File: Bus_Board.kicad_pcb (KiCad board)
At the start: 2 copper layers, 295.9 x 39.4 mm, 44 parts, among them J1 +5V, J10 Conn_02x05_Odd_Even, J11 Conn_02x08_Odd_Even, J12 Conn_02x05_Odd_Even, J13 Conn_02x08_Odd_Even, J14 Conn_02x05_Odd_Even, J15 Conn_02x08_Odd_Even, J16 Conn_02x05_Odd_Even, J17 Conn_02x08_Odd_Even, J18 Conn_02x05_Odd_Even, J19 Conn_02x08_Odd_Even, J2 +12V, J20 Conn_02x05_Odd_Even, J21 Conn_02x08_Odd_Even, J22 Conn_02x05_Odd_Even, J23 Conn_02x08_Odd_Even, J24 Conn_02x05_Odd_Even, J25 +5V, J26 +12V, J27 GND, J28 -12V, J3 GND, J4 -12V, J5 Conn_02x08_Odd_Even, J6 Conn_02x05_Odd_Even, J7 Conn_02x08_Odd_Even, J8 Conn_02x05_Odd_Even, J9 Conn_02x08_Odd_Even

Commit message: Fix orientation of connectors and some other parts
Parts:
- moved J17 18.0 mm to (73.7, 80.0), turned to 180 degrees
- moved J5 18.0 mm to (-101.0, 80.0), turned to 180 degrees
- moved J11 18.0 mm to (-25.4, 80.0), turned to 180 degrees
- moved J13 18.0 mm to (-0.75, 80.0), turned to 180 degrees
- moved J19 18.0 mm to (97.6, 80.0), turned to 180 degrees
- moved J21 18.0 mm to (120.4, 80.0), turned to 180 degrees
- moved J9 18.0 mm to (-50.8, 80.0), turned to 180 degrees
- moved J23 18.0 mm to (143.3, 80.0), turned to 180 degrees
- moved J7 18.0 mm to (-76.2, 80.0), turned to 180 degrees
- moved J15 17.9 mm to (50.2, 80.0), turned to 180 degrees
- moved J24 10.5 mm to (155.5, 80.0), turned to 180 degrees
- moved J12 10.5 mm to (-13.2, 80.0), turned to 180 degrees
- moved J18 10.5 mm to (85.6, 80.0), turned to 180 degrees
- moved J20 10.5 mm to (109.0, 80.0), turned to 180 degrees
- moved J8 10.5 mm to (-63.5, 80.0), turned to 180 degrees
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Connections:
- C3 pad 1: -12V -> GND
- C3 pad 2: GND -> -12V
- D3 pad 1: GND -> Net-(R3-Pad1)
- D3 pad 2: Net-(D3-Pad2) -> GND
- J10 pad 1: +12V -> -12V
- J10 pad 10: -12V -> +12V
- J10 pad 2: +12V -> -12V
- J10 pad 9: -12V -> +12V
- J11 pad 1: Net-(J7-Pad1) -> -12V
- J11 pad 10: GND -> +12V
- J11 pad 11: GND -> +5V
- J11 pad 12: GND -> +5V
- J11 pad 13: GND -> Net-(J11-Pad13)
- J11 pad 14: GND -> Net-(J11-Pad13)
- J11 pad 15: -12V -> Net-(J11-Pad15)
- J11 pad 16: -12V -> Net-(J11-Pad15)
- J11 pad 2: Net-(J7-Pad1) -> -12V
- J11 pad 3: Net-(J7-Pad3) -> GND
- J11 pad 4: Net-(J7-Pad3) -> GND
- J11 pad 5: +5V -> GND
- J11 pad 6: +5V -> GND
- J11 pad 7: +12V -> GND
- J11 pad 8: +12V -> GND
- J11 pad 9: GND -> +12V
- J12 pad 1: +12V -> -12V
- J12 pad 10: -12V -> +12V
- J12 pad 2: +12V -> -12V
- J12 pad 9: -12V -> +12V
- J13 pad 1: Net-(J7-Pad1) -> -12V
- J13 pad 10: GND -> +12V
- J13 pad 11: GND -> +5V
- J13 pad 12: GND -> +5V
- J13 pad 13: GND -> Net-(J11-Pad13)
- J13 pad 14: GND -> Net-(J11-Pad13)
- J13 pad 15: -12V -> Net-(J11-Pad15)
- J13 pad 16: -12V -> Net-(J11-Pad15)
- J13 pad 2: Net-(J7-Pad1) -> -12V
- J13 pad 3: Net-(J7-Pad3) -> GND
- J13 pad 4: Net-(J7-Pad3) -> GND
- J13 pad 5: +5V -> GND
- J13 pad 6: +5V -> GND
- J13 pad 7: +12V -> GND
- J13 pad 8: +12V -> GND
- J13 pad 9: GND -> +12V
- J14 pad 1: +12V -> -12V
- J14 pad 10: -12V -> +12V
- J14 pad 2: +12V -> -12V
- J14 pad 9: -12V -> +12V
- J15 pad 1: Net-(J19-Pad1) -> -12V
- J15 pad 10: GND -> +12V
- J15 pad 11: GND -> +5V
- J15 pad 12: GND -> +5V
- J15 pad 13: GND -> Net-(J15-Pad13)
- J15 pad 14: GND -> Net-(J15-Pad13)
- J15 pad 15: -12V -> Net-(J15-Pad15)
- J15 pad 16: -12V -> Net-(J15-Pad15)
- J15 pad 2: Net-(J19-Pad1) -> -12V
- J15 pad 3: Net-(J19-Pad3) -> GND
- J15 pad 4: Net-(J19-Pad3) -> GND
- J15 pad 5: +5V -> GND
- J15 pad 6: +5V -> GND
- J15 pad 7: +12V -> GND
- J15 pad 8: +12V -> GND
- J15 pad 9: GND -> +12V
- J16 pad 1: +12V -> -12V
- J16 pad 10: -12V -> +12V
- J16 pad 2: +12V -> -12V
- J16 pad 9: -12V -> +12V
- J17 pad 1: Net-(J19-Pad1) -> -12V
- J17 pad 10: GND -> +12V
- J17 pad 11: GND -> +5V
- J17 pad 12: GND -> +5V
- J17 pad 13: GND -> Net-(J15-Pad13)
- J17 pad 14: GND -> Net-(J15-Pad13)
- J17 pad 15: -12V -> Net-(J15-Pad15)
- J17 pad 16: -12V -> Net-(J15-Pad15)
- J17 pad 2: Net-(J19-Pad1) -> -12V
- J17 pad 3: Net-(J19-Pad3) -> GND
- J17 pad 4: Net-(J19-Pad3) -> GND
- J17 pad 5: +5V -> GND
- J17 pad 6: +5V -> GND
- J17 pad 7: +12V -> GND
- J17 pad 8: +12V -> GND
- J17 pad 9: GND -> +12V
- J18 pad 1: +12V -> -12V
- J18 pad 10: -12V -> +12V
- J18 pad 2: +12V -> -12V
- J18 pad 9: -12V -> +12V
- J19 pad 1: Net-(J19-Pad1) -> -12V
- J19 pad 10: GND -> +12V
- J19 pad 11: GND -> +5V
- J19 pad 12: GND -> +5V
- J19 pad 13: GND -> Net-(J15-Pad13)
- J19 pad 14: GND -> Net-(J15-Pad13)
- J19 pad 15: -12V -> Net-(J15-Pad15)
- J19 pad 16: -12V -> Net-(J15-Pad15)
- J19 pad 2: Net-(J19-Pad1) -> -12V
- J19 pad 3: Net-(J19-Pad3) -> GND
- J19 pad 4: Net-(J19-Pad3) -> GND
- J19 pad 5: +5V -> GND
- J19 pad 6: +5V -> GND
- J19 pad 7: +12V -> GND
- J19 pad 8: +12V -> GND
- J19 pad 9: GND -> +12V
- J20 pad 1: +12V -> -12V
- J20 pad 10: -12V -> +12V
- J20 pad 2: +12V -> -12V
- J20 pad 9: -12V -> +12V
- J21 pad 1: Net-(J19-Pad1) -> -12V
- J21 pad 10: GND -> +12V
- J21 pad 11: GND -> +5V
- J21 pad 12: GND -> +5V
- J21 pad 13: GND -> Net-(J15-Pad13)
- J21 pad 14: GND -> Net-(J15-Pad13)
- J21 pad 15: -12V -> Net-(J15-Pad15)
- J21 pad 16: -12V -> Net-(J15-Pad15)
- J21 pad 2: Net-(J19-Pad1) -> -12V
- J21 pad 3: Net-(J19-Pad3) -> GND
- J21 pad 4: Net-(J19-Pad3) -> GND
- J21 pad 5: +5V -> GND
- J21 pad 6: +5V -> GND
- J21 pad 7: +12V -> GND
- J21 pad 8: +12V -> GND
- J21 pad 9: GND -> +12V
- J22 pad 1: +12V -> -12V
- J22 pad 10: -12V -> +12V
- J22 pad 2: +12V -> -12V
- J22 pad 9: -12V -> +12V
- J23 pad 1: Net-(J19-Pad1) -> -12V
- J23 pad 10: GND -> +12V
- J23 pad 11: GND -> +5V
- J23 pad 12: GND -> +5V
- J23 pad 13: GND -> Net-(J15-Pad13)
- J23 pad 14: GND -> Net-(J15-Pad13)
- J23 pad 15: -12V -> Net-(J15-Pad15)
- J23 pad 16: -12V -> Net-(J15-Pad15)
- J23 pad 2: Net-(J19-Pad1) -> -12V
- J23 pad 3: Net-(J19-Pad3) -> GND
- J23 pad 4: Net-(J19-Pad3) -> GND
- J23 pad 5: +5V -> GND
- J23 pad 6: +5V -> GND
- J23 pad 7: +12V -> GND
- J23 pad 8: +12V -> GND
- J23 pad 9: GND -> +12V
- J24 pad 1: +12V -> -12V
- J24 pad 10: -12V -> +12V
- J24 pad 2: +12V -> -12V
- J24 pad 9: -12V -> +12V
- J5 pad 1: Net-(J7-Pad1) -> -12V
- J5 pad 10: GND -> +12V
- J5 pad 11: GND -> +5V
- J5 pad 12: GND -> +5V
- J5 pad 13: GND -> Net-(J11-Pad13)
- J5 pad 14: GND -> Net-(J11-Pad13)
- J5 pad 15: -12V -> Net-(J11-Pad15)
- J5 pad 16: -12V -> Net-(J11-Pad15)
- J5 pad 2: Net-(J7-Pad1) -> -12V
- J5 pad 3: Net-(J7-Pad3) -> GND
- J5 pad 4: Net-(J7-Pad3) -> GND
- J5 pad 5: +5V -> GND
- J5 pad 6: +5V -> GND
- J5 pad 7: +12V -> GND
- J5 pad 8: +12V -> GND
- J5 pad 9: GND -> +12V
- J6 pad 1: +12V -> -12V
- J6 pad 10: -12V -> +12V
- J6 pad 2: +12V -> -12V
- J6 pad 9: -12V -> +12V
- J7 pad 1: Net-(J7-Pad1) -> -12V
- J7 pad 10: GND -> +12V
- J7 pad 11: GND -> +5V
- J7 pad 12: GND -> +5V
- J7 pad 13: GND -> Net-(J11-Pad13)
- J7 pad 14: GND -> Net-(J11-Pad13)
- J7 pad 15: -12V -> Net-(J11-Pad15)
- J7 pad 16: -12V -> Net-(J11-Pad15)
- J7 pad 2: Net-(J7-Pad1) -> -12V
- J7 pad 3: Net-(J7-Pad3) -> GND
- J7 pad 4: Net-(J7-Pad3) -> GND
- J7 pad 5: +5V -> GND
- J7 pad 6: +5V -> GND
- J7 pad 7: +12V -> GND
- J7 pad 8: +12V -> GND
- J7 pad 9: GND -> +12V
- J8 pad 1: +12V -> -12V
- J8 pad 10: -12V -> +12V
- J8 pad 2: +12V -> -12V
- J8 pad 9: -12V -> +12V
- J9 pad 1: Net-(J7-Pad1) -> -12V
- J9 pad 10: GND -> +12V
- J9 pad 11: GND -> +5V
- J9 pad 12: GND -> +5V
- J9 pad 13: GND -> Net-(J11-Pad13)
- J9 pad 14: GND -> Net-(J11-Pad13)
- J9 pad 15: -12V -> Net-(J11-Pad15)
- J9 pad 16: -12V -> Net-(J11-Pad15)
- J9 pad 2: Net-(J7-Pad1) -> -12V
- J9 pad 3: Net-(J7-Pad3) -> GND
- J9 pad 4: Net-(J7-Pad3) -> GND
- J9 pad 5: +5V -> GND
- J9 pad 6: +5V -> GND
- J9 pad 7: +12V -> GND
- J9 pad 8: +12V -> GND
- J9 pad 9: GND -> +12V
- R3 pad 1: Net-(D3-Pad2) -> Net-(R3-Pad1)
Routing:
- net Net-(J7-Pad3): track 102.9 -> 0.00 mm
- net Net-(J7-Pad1): track 102.9 -> 0.00 mm
- net Net-(J11-Pad15): track 0.00 -> 102.9 mm
- net Net-(J11-Pad13): track 0.00 -> 102.9 mm
- net Net-(J19-Pad3): track 95.2 -> 0.00 mm
- net Net-(J19-Pad1): track 95.2 -> 0.00 mm
- net Net-(J15-Pad15): track 0.00 -> 95.2 mm
- net Net-(J15-Pad13): track 0.00 -> 95.2 mm
- net Net-(R3-Pad1): track 0.00 -> 6.76 mm
- net Net-(D3-Pad2): track 6.76 -> 0.00 mm

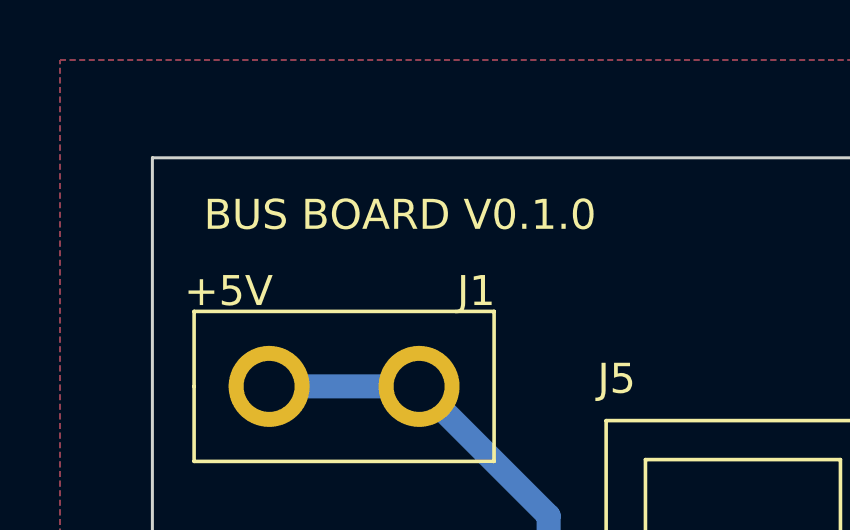
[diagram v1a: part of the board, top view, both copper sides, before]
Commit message: Fix Bug, add thermal reliefs to groundplane
Bugfix: reverse polarity of C3 and D3
Add thermal reliefs in ground plane for easier soldering
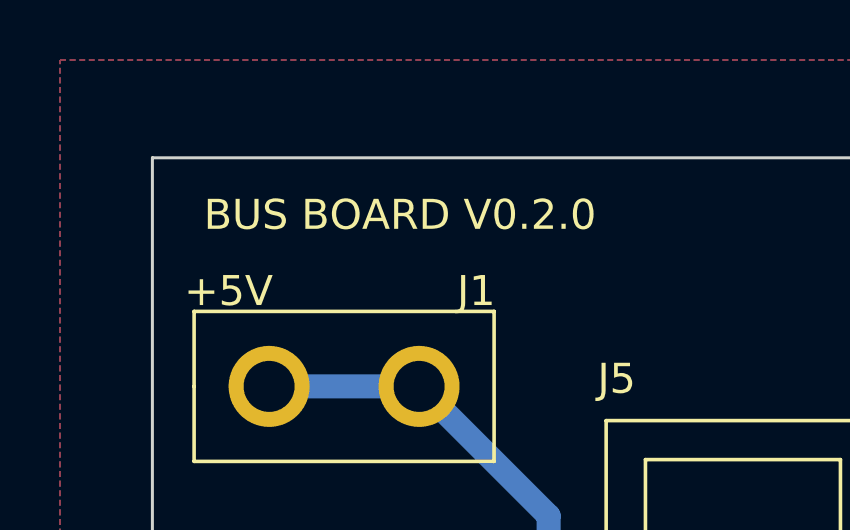
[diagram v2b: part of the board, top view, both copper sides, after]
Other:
- board text added: "BUS BOARD V0.2.0"
- board text removed: "BUS BOARD V0.1.0"
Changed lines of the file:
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@@
     (effects (font (size 1 1) (thickness 0.15)))
   )
-  (gr_text "BUS BOARD V0.1.0" (at -113.665 50.165) (layer "F.SilkS")
+  (gr_text "BUS BOARD V0.2.0" (at -113.665 50.165) (layer "F.SilkS")
     (effects (font (size 1 1) (thickness 0.15)))
   )
@@
     (connect_pads (clearance 0.508))
     (min_thickness 0.254) (filled_areas_thickness no)
-    (fill yes (thermal_gap 0.508) (thermal_bridge_width 0.508))
+    (fill (thermal_gap 0.508) (thermal_bridge_width 0.508))
     (polygon
       (pts

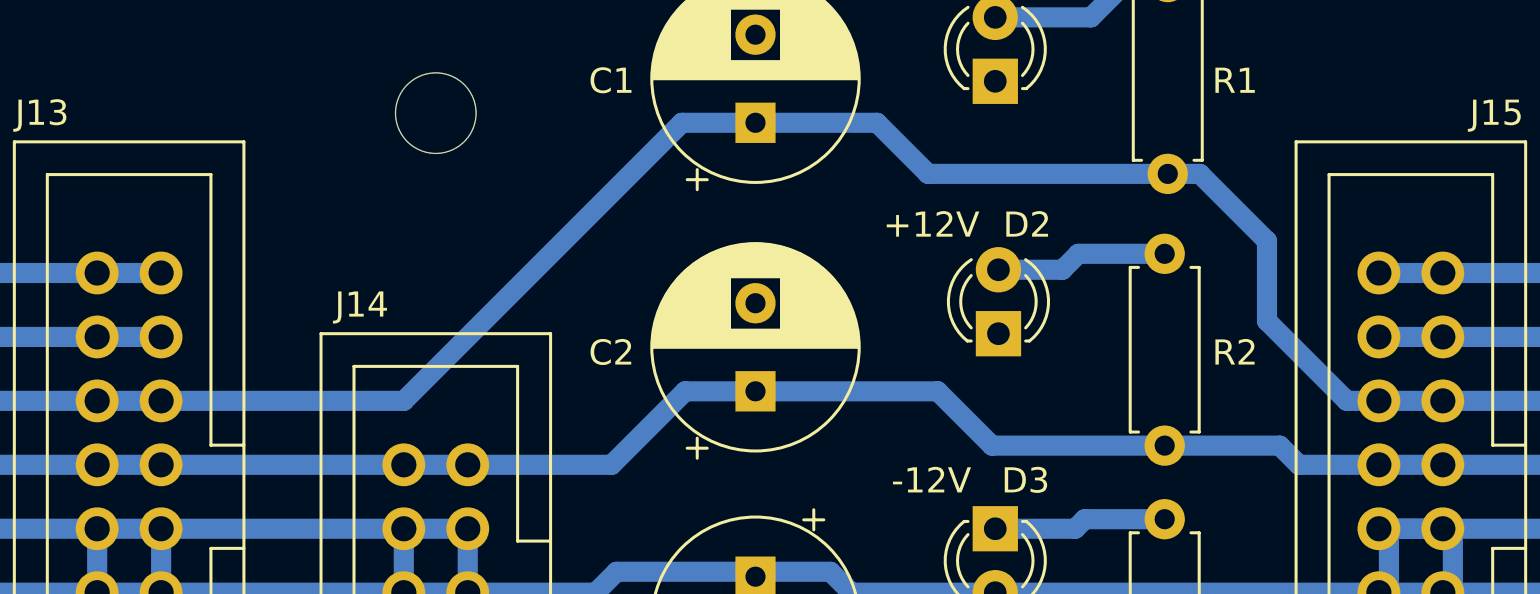
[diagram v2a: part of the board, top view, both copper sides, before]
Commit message: Connect CV and GATE lines, add ljcpcb order number
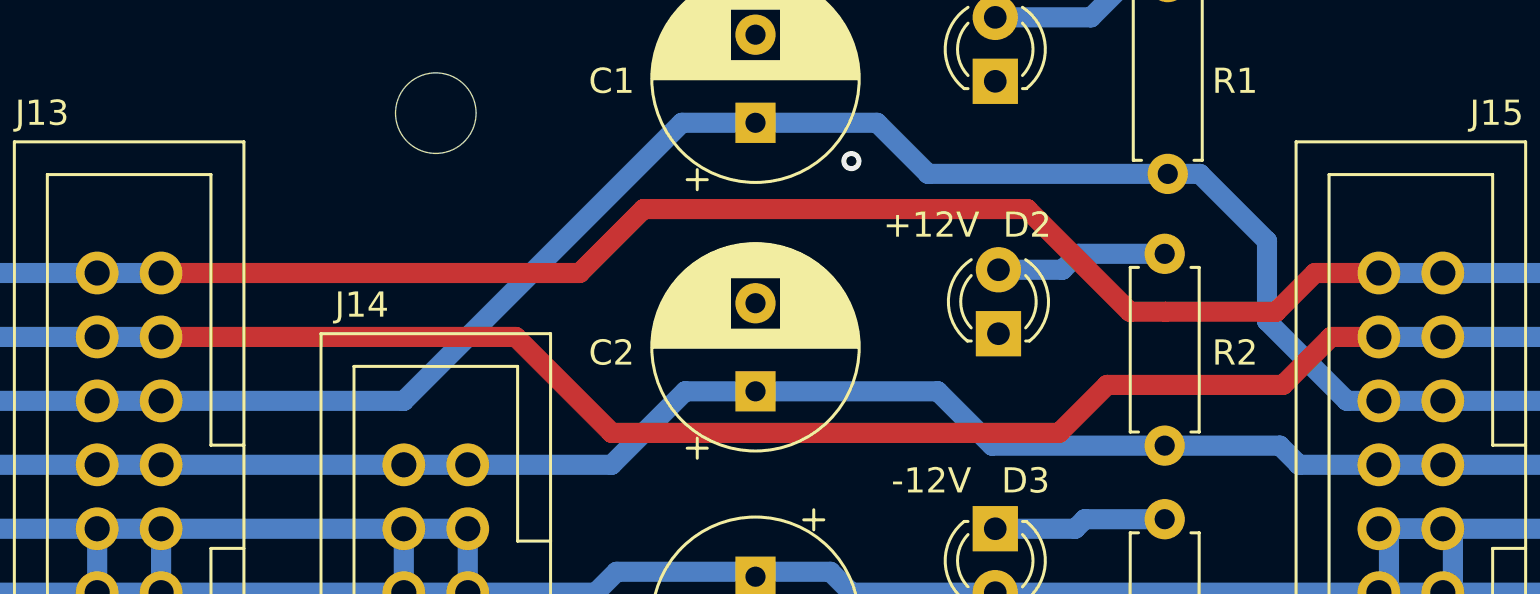
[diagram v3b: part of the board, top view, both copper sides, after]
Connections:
- J11 pad 13: Net-(J11-Pad13) -> CV
- J11 pad 14: Net-(J11-Pad13) -> CV
- J11 pad 15: Net-(J11-Pad15) -> GATE
- J11 pad 16: Net-(J11-Pad15) -> GATE
- J13 pad 13: Net-(J11-Pad13) -> CV
- J13 pad 14: Net-(J11-Pad13) -> CV
- J13 pad 15: Net-(J11-Pad15) -> GATE
- J13 pad 16: Net-(J11-Pad15) -> GATE
- J15 pad 13: Net-(J15-Pad13) -> CV
- J15 pad 14: Net-(J15-Pad13) -> CV
- J15 pad 15: Net-(J15-Pad15) -> GATE
- J15 pad 16: Net-(J15-Pad15) -> GATE
- J17 pad 13: Net-(J15-Pad13) -> CV
- J17 pad 14: Net-(J15-Pad13) -> CV
- J17 pad 15: Net-(J15-Pad15) -> GATE
- J17 pad 16: Net-(J15-Pad15) -> GATE
- J19 pad 13: Net-(J15-Pad13) -> CV
- J19 pad 14: Net-(J15-Pad13) -> CV
- J19 pad 15: Net-(J15-Pad15) -> GATE
- J19 pad 16: Net-(J15-Pad15) -> GATE
- J21 pad 13: Net-(J15-Pad13) -> CV
- J21 pad 14: Net-(J15-Pad13) -> CV
- J21 pad 15: Net-(J15-Pad15) -> GATE
- J21 pad 16: Net-(J15-Pad15) -> GATE
- J23 pad 13: Net-(J15-Pad13) -> CV
- J23 pad 14: Net-(J15-Pad13) -> CV
- J23 pad 15: Net-(J15-Pad15) -> GATE
- J23 pad 16: Net-(J15-Pad15) -> GATE
- J5 pad 13: Net-(J11-Pad13) -> CV
- J5 pad 14: Net-(J11-Pad13) -> CV
- J5 pad 15: Net-(J11-Pad15) -> GATE
- J5 pad 16: Net-(J11-Pad15) -> GATE
- J7 pad 13: Net-(J11-Pad13) -> CV
- J7 pad 14: Net-(J11-Pad13) -> CV
- J7 pad 15: Net-(J11-Pad15) -> GATE
- J7 pad 16: Net-(J11-Pad15) -> GATE
- J9 pad 13: Net-(J11-Pad13) -> CV
- J9 pad 14: Net-(J11-Pad13) -> CV
- J9 pad 15: Net-(J11-Pad15) -> GATE
- J9 pad 16: Net-(J11-Pad15) -> GATE
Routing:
- net GATE: track 0.00 -> 249.9 mm
- net CV: track 0.00 -> 249.7 mm
- net Net-(J11-Pad15): track 102.9 -> 0.00 mm
- net Net-(J11-Pad13): track 102.9 -> 0.00 mm
- net Net-(J15-Pad15): track 95.2 -> 0.00 mm
- net Net-(J15-Pad13): track 95.2 -> 0.00 mm
- net GND: vias 0 -> 1
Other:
- board text added: "JLCJLCJLCJLC"
